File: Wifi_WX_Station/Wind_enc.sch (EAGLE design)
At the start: 9 parts, among them U1 AS5030

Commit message: updated BOM with all prices- As Checked in to BATCH PCB
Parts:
- +5V, GND, OUT: value LSP10 -> TPSOL; device solpad:LSP10 -> wifi_WX:TPSOL
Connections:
- net N$1: now also +5V.P$1; no longer +5V.MP
- net N$2: now also GND.P$1; no longer GND.MP
- net N$22: now also OUT.P$1; no longer OUT.MP

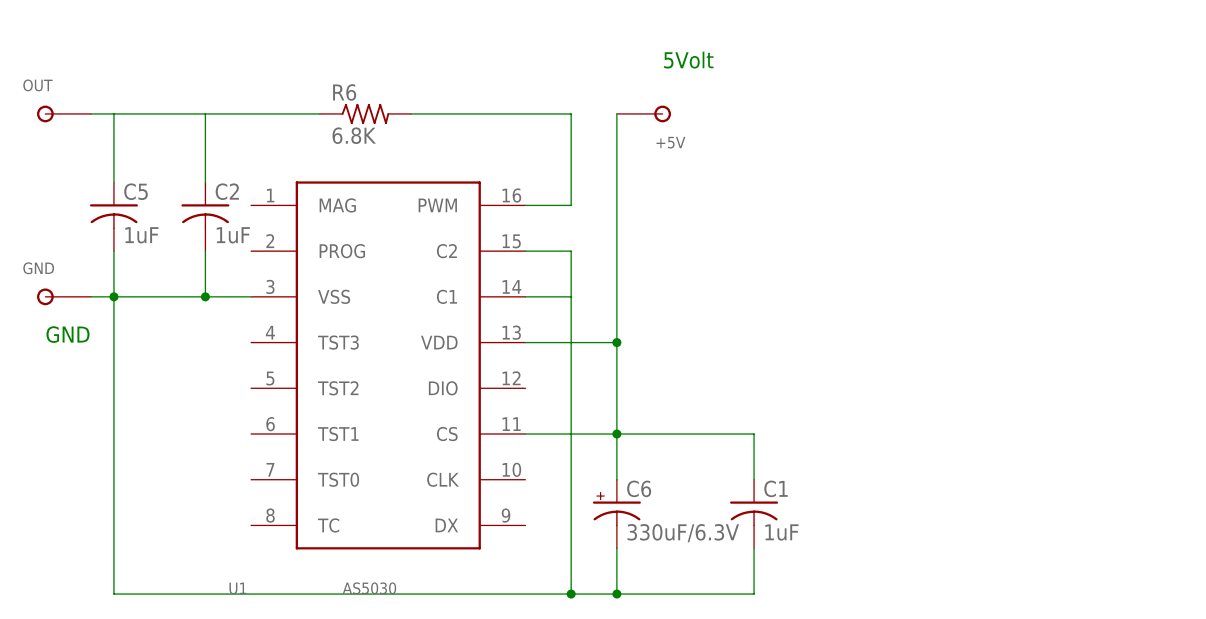
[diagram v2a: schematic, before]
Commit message: 
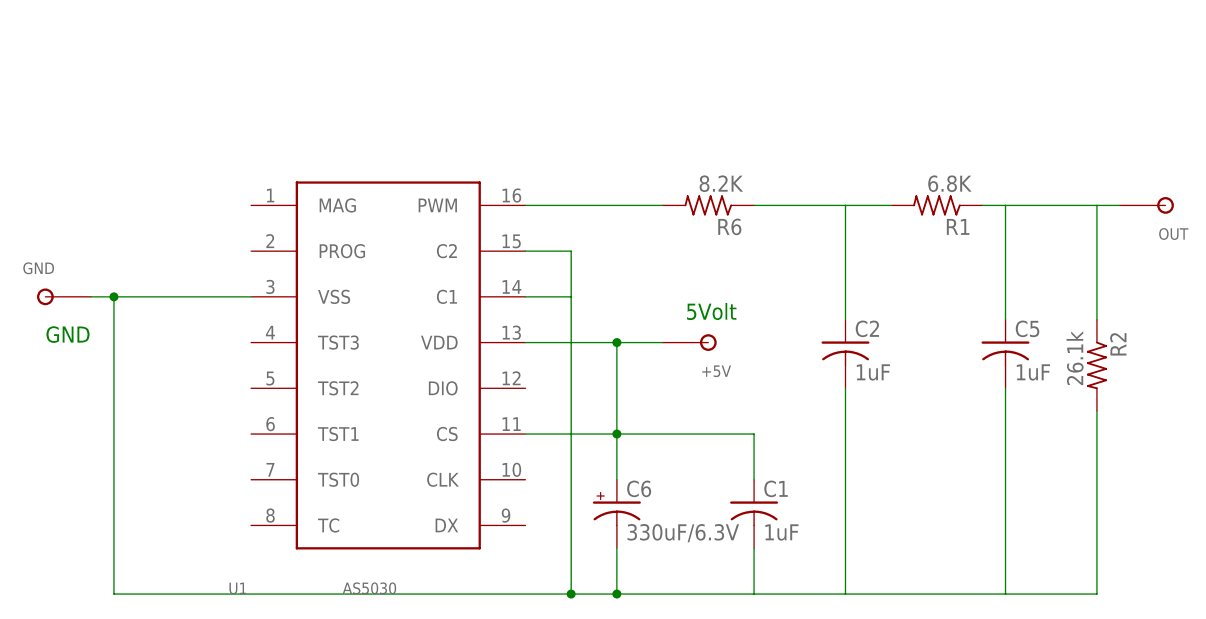
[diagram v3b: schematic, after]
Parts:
- added R1: 6.8K, rcl:R-US_R0603
- added R2: 26.1k, rcl:R-US_R0603
- R6: value 6.8K -> 8.2K; device rcl:R-US_M0805 -> rcl:R-US_R0603
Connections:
- new net N$3: C5.1, OUT.P$1, R1.1, R2.1
- net N$2: now also R2.2
- net N$22: now also R1.2; no longer C5.1, OUT.P$1
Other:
- moved on the sheet: +5V, C2, C5, OUT, R6
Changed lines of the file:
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@@
 <layer number="254" name="cooling" color="7" fill="1" visible="yes" active="yes"/>
 </layers>
-<schematic>
+<schematic xreflabel="%F%N/%S.%C%R" xrefpart="/%S.%C%R">
 <attributes>
 </attributes>
@@
 <parts>
 <part name="U1" library="Stofer" deviceset="AS5030" device=""/>
-<part name="R6" library="rcl" deviceset="R-US_" device="M0805" value="6.8K"/>
+<part name="R6" library="rcl" deviceset="R-US_" device="R0603" value="8.2K"/>
 <part name="C5" library="rcl" deviceset="C-US" device="C0805K" value="1uF"/>
 <part name="C6" library="rcl" deviceset="CPOL-US" device="SMCD" value="330uF/6.3V"/>
@@
 <part name="+5V" library="wifi_WX" deviceset="TP" device="SOL"/>
 <part name="GND" library="wifi_WX" deviceset="TP" device="SOL"/>
+<part name="R1" library="rcl" deviceset="R-US_" device="R0603" value="6.8K"/>
+<part name="R2" library="rcl" deviceset="R-US_" device="R0603" value="26.1k"/>
 </parts>
 <sheets>
 <sheet>
 <plain>
-<text x="38.1" y="96.52" size="1.778" layer="91">5Volt</text>
+<text x="40.64" y="68.58" size="1.778" layer="91">5Volt</text>
 <text x="-30.48" y="66.04" size="1.778" layer="91">GND</text>
 </plain>
 <instances>
 <instance part="U1" gate="G$1" x="7.62" y="55.88"/>
-<instance part="R6" gate="G$1" x="5.08" y="91.44"/>
-<instance part="C5" gate="G$1" x="-22.86" y="81.28"/>
+<instance part="R6" gate="G$1" x="43.18" y="81.28" rot="R180"/>
+<instance part="C5" gate="G$1" x="76.2" y="66.04"/>
 <instance part="C6" gate="G$1" x="33.02" y="48.26"/>
 <instance part="C1" gate="G$1" x="48.26" y="48.26"/>
-<instance part="C2" gate="G$1" x="-12.7" y="81.28"/>
-<instance part="OUT" gate="G$1" x="-30.48" y="91.44"/>
-<instance part="+5V" gate="G$1" x="38.1" y="91.44" rot="R180"/>
+<instance part="C2" gate="G$1" x="58.42" y="66.04"/>
+<instance part="OUT" gate="G$1" x="93.98" y="81.28" rot="R180"/>
+<instance part="+5V" gate="G$1" x="43.18" y="66.04" rot="R180"/>
 <instance part="GND" gate="G$1" x="-30.48" y="71.12"/>
+<instance part="R1" gate="G$1" x="68.58" y="81.28" rot="R180"/>
+<instance part="R2" gate="G$1" x="86.36" y="63.5" rot="R270"/>
 </instances>
 <busses>
@@
 <net name="N$22" class="0">
 <segment>
-<wire x1="-22.86" y1="91.44" x2="-12.7" y2="91.44" width="0.1524" layer="91"/>
-<wire x1="-12.7" y1="91.44" x2="0" y2="91.44" width="0.1524" layer="91"/>
-<wire x1="-22.86" y1="83.82" x2="-22.86" y2="91.44" width="0.1524" layer="91"/>
-<wire x1="-22.86" y1="91.44" x2="-25.4" y2="91.44" width="0.1524" layer="91"/>
-<wire x1="-12.7" y1="83.82" x2="-12.7" y2="91.44" width="0.1524" layer="91"/>
+<wire x1="58.42" y1="81.28" x2="48.26" y2="81.28" width="0.1524" layer="91"/>
+<wire x1="58.42" y1="68.58" x2="58.42" y2="81.28" width="0.1524" layer="91"/>
 <pinref part="R6" gate="G$1" pin="1"/>
-<pinref part="C5" gate="G$1" pin="1"/>
 <pinref part="C2" gate="G$1" pin="1"/>
-<pinref part="OUT" gate="G$1" pin="P$1"/>
+<pinref part="R1" gate="G$1" pin="2"/>
+<wire x1="58.42" y1="81.28" x2="63.5" y2="81.28" width="0.1524" layer="91"/>
 </segment>
 </net>
 <net name="N$23" class="0">
 <segment>
-<wire x1="10.16" y1="91.44" x2="27.94" y2="91.44" width="0.1524" layer="91"/>
-<wire x1="27.94" y1="91.44" x2="27.94" y2="81.28" width="0.1524" layer="91"/>
-<wire x1="27.94" y1="81.28" x2="22.86" y2="81.28" width="0.1524" layer="91"/>
+<wire x1="38.1" y1="81.28" x2="22.86" y2="81.28" width="0.1524" layer="91"/>
 <pinref part="R6" gate="G$1" pin="2"/>
 <pinref part="U1" gate="G$1" pin="PWM"/>
@@
 <net name="N$1" class="0">
 <segment>
-<wire x1="33.02" y1="91.44" x2="33.02" y2="66.04" width="0.1524" layer="91"/>
+<wire x1="38.1" y1="66.04" x2="33.02" y2="66.04" width="0.1524" layer="91"/>
 <wire x1="33.02" y1="66.04" x2="22.86" y2="66.04" width="0.1524" layer="91"/>
 <wire x1="33.02" y1="66.04" x2="33.02" y2="55.88" width="0.1524" layer="91"/>
@@
 <wire x1="33.02" y1="38.1" x2="27.94" y2="38.1" width="0.1524" layer="91"/>
 <wire x1="27.94" y1="38.1" x2="-22.86" y2="38.1" width="0.1524" layer="91"/>
-<wire x1="-7.62" y1="71.12" x2="-12.7" y2="71.12" width="0.1524" layer="91"/>
-<wire x1="-12.7" y1="71.12" x2="-22.86" y2="71.12" width="0.1524" layer="91"/>
-<wire x1="-22.86" y1="76.2" x2="-22.86" y2="71.12" width="0.1524" layer="91"/>
+<wire x1="-7.62" y1="71.12" x2="-22.86" y2="71.12" width="0.1524" layer="91"/>
 <wire x1="-25.4" y1="71.12" x2="-22.86" y2="71.12" width="0.1524" layer="91"/>
 <wire x1="-22.86" y1="71.12" x2="-22.86" y2="38.1" width="0.1524" layer="91"/>
-<wire x1="-12.7" y1="76.2" x2="-12.7" y2="71.12" width="0.1524" layer="91"/>
 <junction x="-22.86" y="71.12"/>
 <junction x="27.94" y="38.1"/>
 <junction x="33.02" y="38.1"/>
-<junction x="-12.7" y="71.12"/>
 <pinref part="U1" gate="G$1" pin="C1"/>
 <pinref part="U1" gate="G$1" pin="C2"/>
@@
 <pinref part="C1" gate="G$1" pin="2"/>
 <pinref part="U1" gate="G$1" pin="VSS"/>
+<pinref part="GND" gate="G$1" pin="P$1"/>
 <pinref part="C5" gate="G$1" pin="2"/>
+<wire x1="48.26" y1="38.1" x2="58.42" y2="38.1" width="0.1524" layer="91"/>
+<wire x1="58.42" y1="38.1" x2="76.2" y2="38.1" width="0.1524" layer="91"/>
+<wire x1="76.2" y1="38.1" x2="76.2" y2="60.96" width="0.1524" layer="91"/>
 <pinref part="C2" gate="G$1" pin="2"/>
-<pinref part="GND" gate="G$1" pin="P$1"/>
+<wire x1="58.42" y1="60.96" x2="58.42" y2="38.1" width="0.1524" layer="91"/>
+<pinref part="R2" gate="G$1" pin="2"/>
+<wire x1="76.2" y1="38.1" x2="86.36" y2="38.1" width="0.1524" layer="91"/>
+<wire x1="86.36" y1="38.1" x2="86.36" y2="58.42" width="0.1524" layer="91"/>
 </segment>
 </net>
+<net name="N$3" class="0">
+<segment>
+<pinref part="OUT" gate="G$1" pin="P$1"/>
+<wire x1="76.2" y1="81.28" x2="86.36" y2="81.28" width="0.1524" layer="91"/>
+<wire x1="86.36" y1="81.28" x2="88.9" y2="81.28" width="0.1524" layer="91"/>
+<wire x1="76.2" y1="68.58" x2="76.2" y2="81.28" width="0.1524" layer="91"/>
+<pinref part="C5" gate="G$1" pin="1"/>
+<pinref part="R1" gate="G$1" pin="1"/>
+<wire x1="73.66" y1="81.28" x2="76.2" y2="81.28" width="0.1524" layer="91"/>
+<pinref part="R2" gate="G$1" pin="1"/>
+<wire x1="86.36" y1="68.58" x2="86.36" y2="81.28" width="0.1524" layer="91"/>
+</segment>
+</net>
